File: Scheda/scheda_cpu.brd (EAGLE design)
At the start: 75 x 70 mm, 36 parts, among them IC2 LM3801N, IC3 LD1117V33

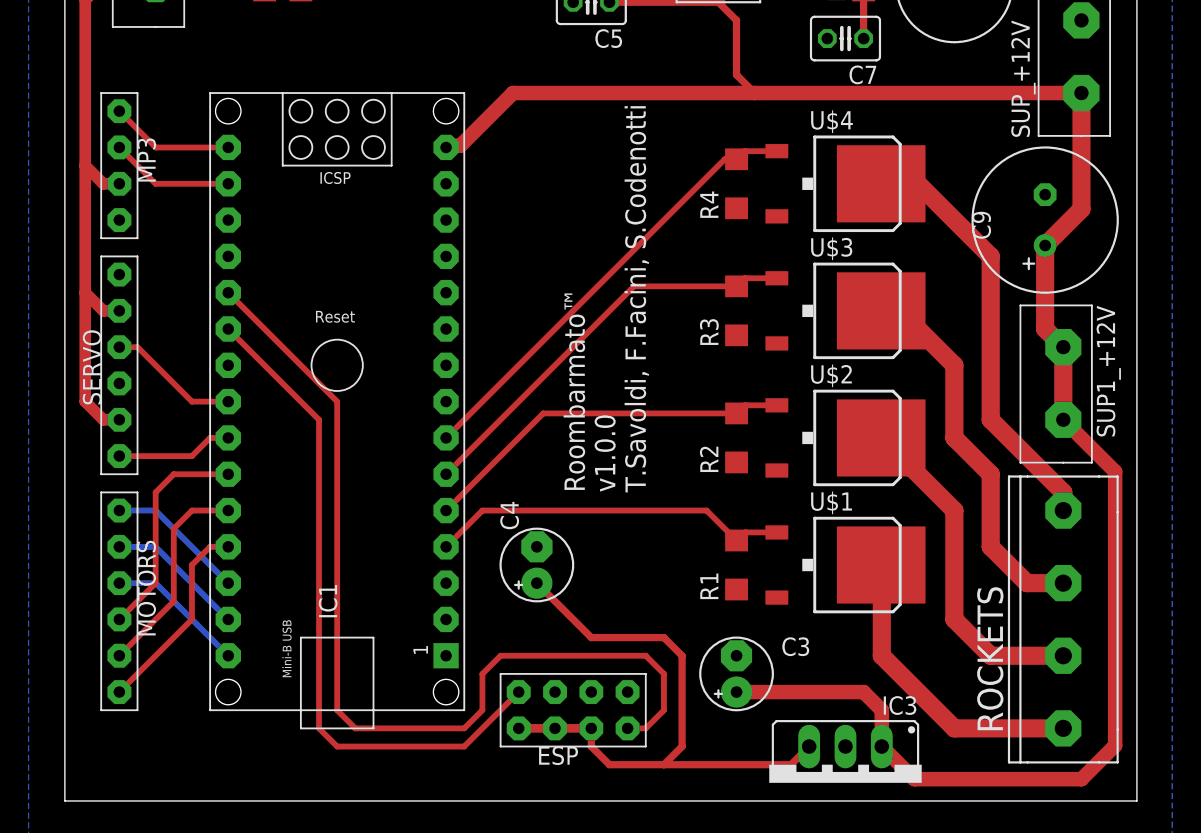
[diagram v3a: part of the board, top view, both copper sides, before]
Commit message: aggiunte etichette su pcb
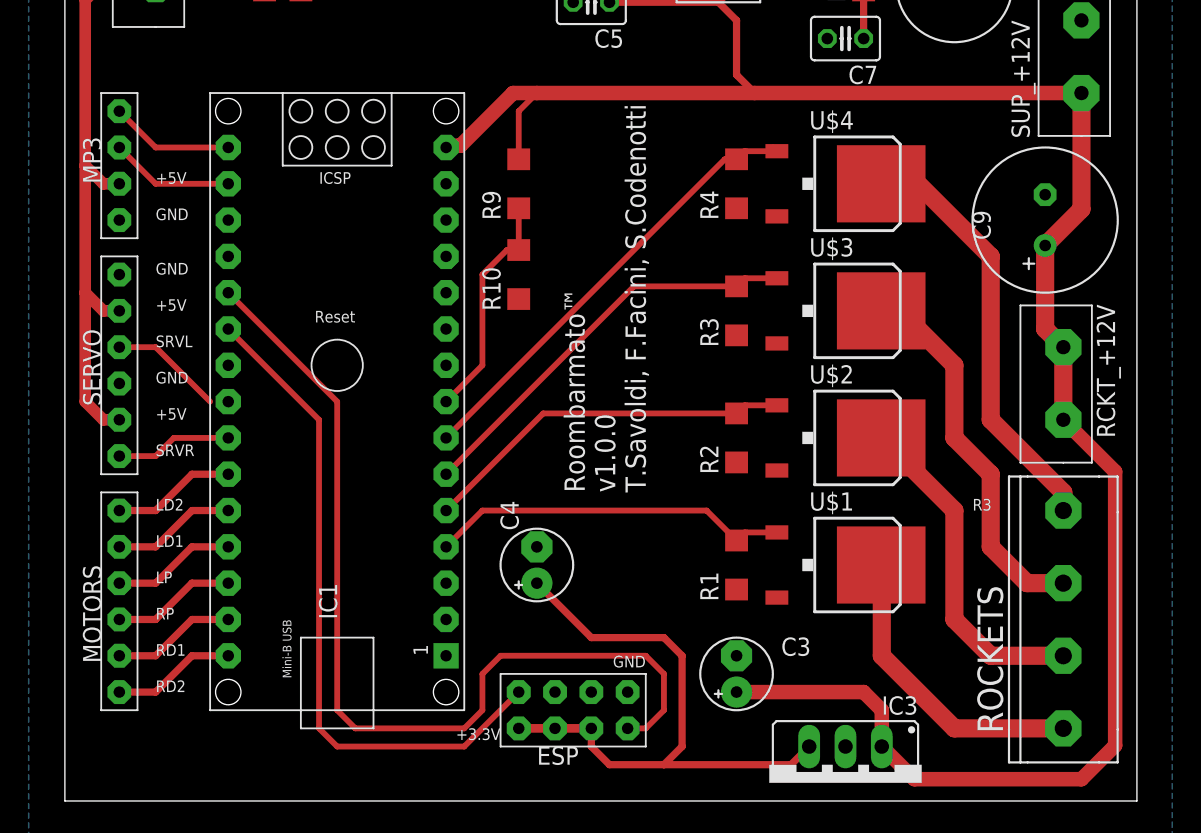
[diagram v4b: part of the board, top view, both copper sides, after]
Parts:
- added R10: 100k, roombarmato_eagle_lib:1206-RESISTOR
- added R9: 200k, roombarmato_eagle_lib:1206-RESISTOR
- turned MOTORS to 270 degrees
- renumbered SUP1_+12V to RCKT_+12V
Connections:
- net N$13 renamed LD1
- net N$16 renamed RD1
- net N$2 renamed TXD
- net N$3 renamed RXD
- net SERVO1 renamed SRV_L
- net SERVO2 renamed SRV_R
- removed net N$11: IC1.28, MOTORS.P$6
- removed net N$12: IC1.27, MOTORS.P$1
- removed net N$14: IC1.25, MOTORS.P$3
- removed net N$15: IC1.30, MOTORS.P$4
- new net CHK_VBAT: IC1.8, R10.P$2, R9.P$1
- new net LD2: IC1.25, MOTORS.P$1
- new net LP: IC1.27, MOTORS.P$3
- new net RD2: IC1.30, MOTORS.P$6
- new net RP: IC1.28, MOTORS.P$4
- net +12V: now also R9.P$2
- net GND: now also R10.P$1
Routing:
- net CHK_VBAT: track 0.00 -> 16.1 mm
- net N$14: track 15.5 -> 0.00 mm
- net N$12: track 14.1 -> 0.00 mm
- net N$15: track 9.72 -> 0.00 mm
- net N$11: track 9.72 -> 0.00 mm
- net RP: track 0.00 -> 8.67 mm
- net LP: track 0.00 -> 8.67 mm
- net RD2: track 0.00 -> 8.67 mm
- net LD2: track 0.00 -> 8.67 mm
- net LD1: track 14.8 -> 8.67 mm
- net +12V: track 149.9 -> 155.1 mm
- net SRV_L: track 9.20 -> 7.93 mm
- net RD1: track 9.72 -> 8.67 mm
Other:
- board text added: "+3.3V"
- board text added: "+5V"
- board text added: "GND"
- board text added: "LD1"
- board text added: "LD2"
- board text added: "LP"
- board text added: "R3"
- board text added: "RD1"
- board text added: "RD2"
- board text added: "RP"
- board text added: "SRVL"
- board text added: "SRVR"

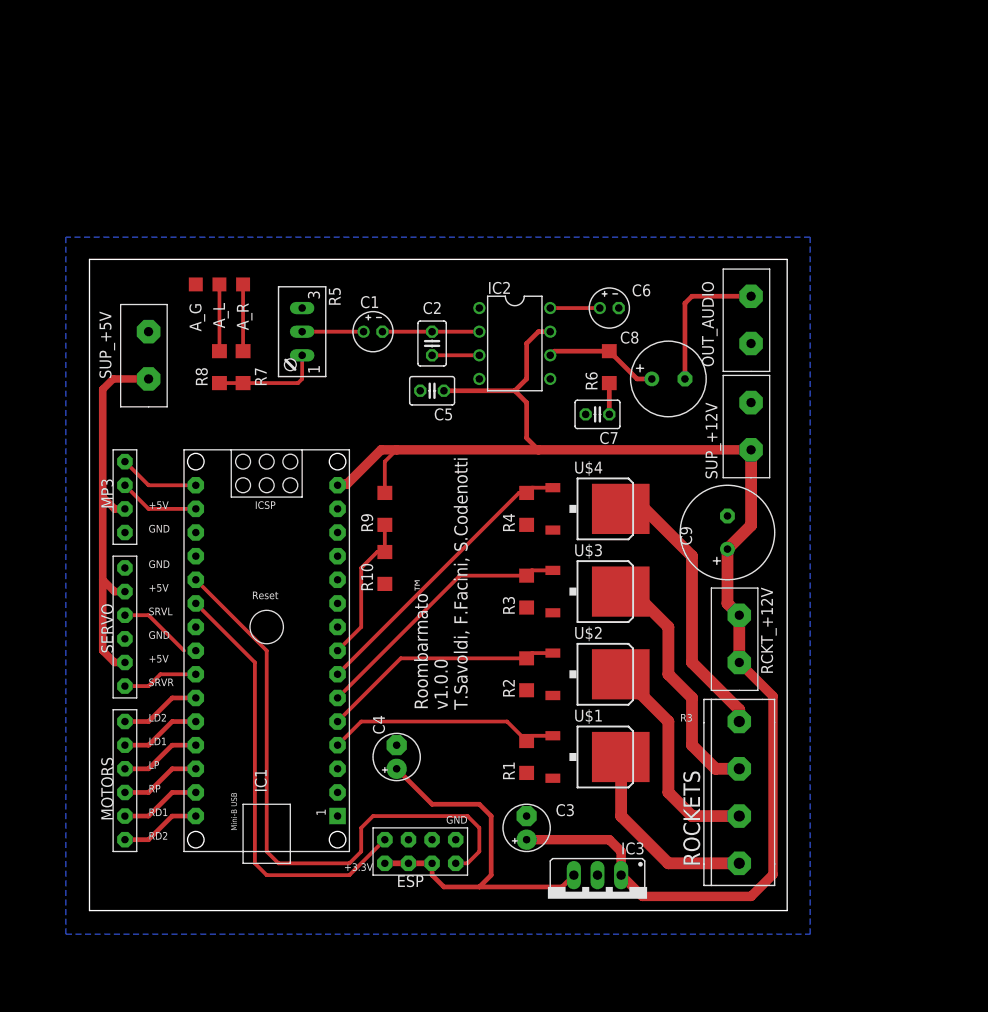
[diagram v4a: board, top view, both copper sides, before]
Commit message: create le cartelle test e ex
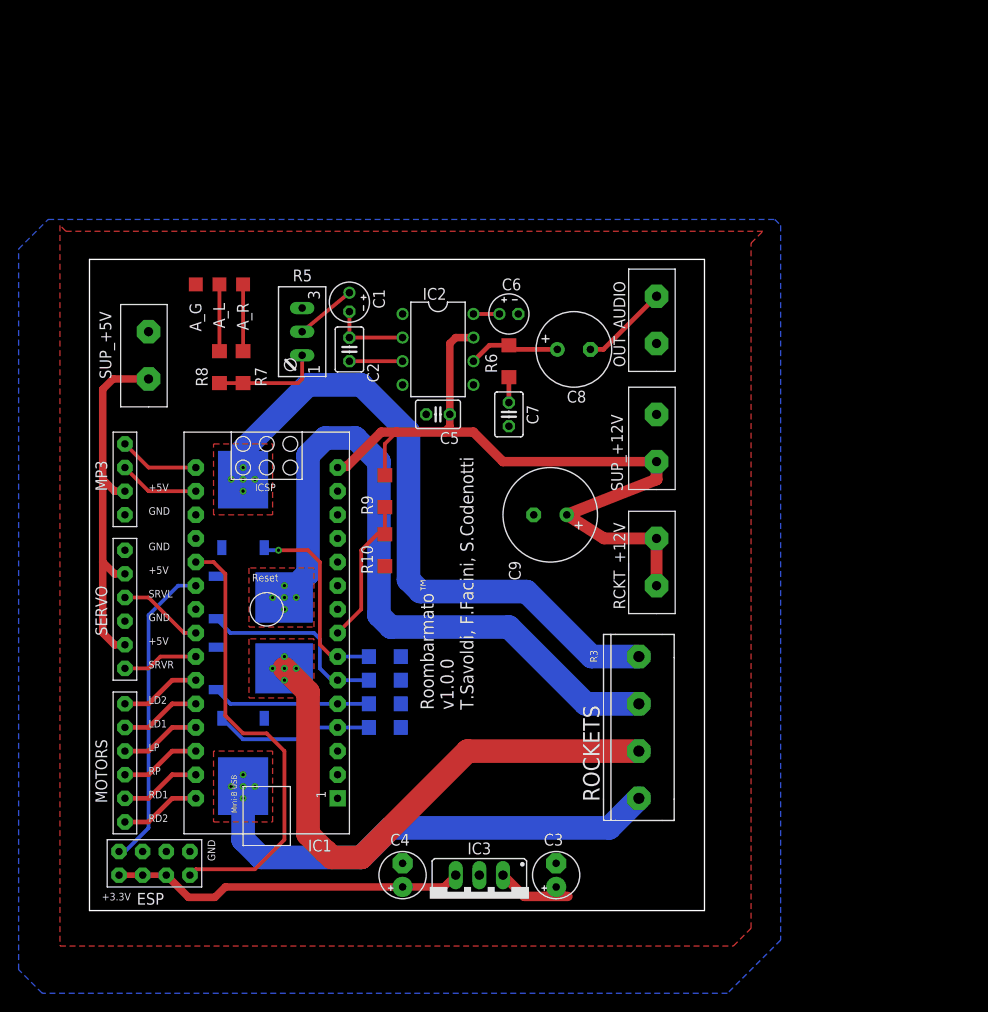
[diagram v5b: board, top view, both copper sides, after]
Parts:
- moved U$1 38.1 mm to (16.5, 15.9), flipped to the bottom, turned to 180 degrees
- moved U$4 38.1 mm to (16.5, 43.8), flipped to the bottom, turned to 0 degrees
- moved U$2 36.2 mm to (18.4, 26.0), flipped to the bottom, turned to 90 degrees
- moved U$3 36.2 mm to (18.4, 33.7), flipped to the bottom, turned to 90 degrees
- moved ESP 28.6 mm to (6.99, 5.08)
- moved R4 22.0 mm to (31.8, 27.3), flipped to the bottom, turned to 0 degrees
- moved C9 19.1 mm to (49.5, 42.5), turned to 180 degrees
- moved R3 18.0 mm to (31.8, 24.8), flipped to the bottom, turned to 0 degrees
- moved R1 15.6 mm to (31.8, 19.7), flipped to the bottom, turned to 0 degrees
- moved R2 15.6 mm to (31.8, 22.2), flipped to the bottom, turned to 0 degrees
- moved ROCKETS 12.9 mm to (59.1, 19.7)
- moved C4 12.7 mm to (33.7, 3.81)
- moved IC3 12.7 mm to (41.9, 1.27)
- moved RCKT_+12V 12.1 mm to (61.0, 34.9)
- moved R6 10.8 mm to (45.1, 59.1)
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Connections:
- new net LED: IC1.9
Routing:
- net +12V: track 155.1 -> 94.0 mm
- net R2: track 30.1 -> 74.2 mm, vias 0 -> 5
- net R3: track 31.4 -> 70.1 mm, vias 0 -> 5
- net R1: track 23.5 -> 60.2 mm, vias 0 -> 5
- net R0: track 21.2 -> 51.7 mm, vias 0 -> 5
- net N$4: track 65.5 -> 48.1 mm
- net N$1: track 46.6 -> 33.5 mm
- net C_R3: track 31.8 -> 21.3 mm, vias 0 -> 1
- net C_R1: track 26.2 -> 17.1 mm
- net C_R0: track 25.3 -> 17.3 mm
- net C_R2: track 28.8 -> 21.0 mm
- net N$17: track 15.6 -> 9.48 mm
- net +3.3V: track 43.1 -> 38.2 mm
- net N$8: track 5.33 -> 2.79 mm
- net N$10: track 12.3 -> 9.91 mm
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- added copper zone on layer 1, net +12V
- added copper zone on layer 1, net R0
- added copper zone on layer 1, net R1
- added copper zone on layer 1, net R2
- added copper zone on layer 1, net R3
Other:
- board size 75 x 70 mm -> 66.1 x 70 mm

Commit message: modificato pcb
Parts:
- added H1, H2, H3: MOUNT-HOLE3.0, ITIS:3,0
- added LED: AK500, roombarmato_eagle_lib:AK500-2
- moved U$4 37.1 mm to (52.7, 35.6), flipped to the top, turned to 270 degrees
- moved U$1 36.3 mm to (52.7, 12.7), flipped to the top, turned to 270 degrees
- moved U$2 34.8 mm to (52.7, 20.3), flipped to the top, turned to 270 degrees
- moved U$3 34.8 mm to (52.7, 27.9), flipped to the top, turned to 270 degrees
- moved R5 31.1 mm to (45.7, 81.9)
- moved A_G 31.1 mm to (35.6, 87.0)
- moved A_L 31.1 mm to (38.1, 87.0)
- moved C7 31.1 mm to (69.2, 73.0)
- moved C8 31.1 mm to (76.2, 80.0)
- moved R8 31.1 mm to (38.1, 78.1)
- moved A_R 31.1 mm to (40.6, 87.0)
- moved C1 31.1 mm to (52.1, 85.1)
- moved C2 31.1 mm to (52.1, 80.0)
- moved R6 31.1 mm to (69.2, 78.7)
- moved R7 31.1 mm to (40.6, 78.1)
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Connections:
- net CHK_VBAT: now also IC1.9; no longer IC1.8
- net GND: now also LED.P$1
- net LED: now also IC1.8, LED.P$2; no longer IC1.9
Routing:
- net +12V: track 94.0 -> 5.42 mm
- net LED: track 0.00 -> 77.1 mm
- net R3: track 70.1 -> 35.9 mm
- net R2: track 74.2 -> 41.2 mm
- net R1: track 60.2 -> 40.0 mm
- net N$4: track 48.1 -> 68.1 mm
- net N$1: track 33.5 -> 50.4 mm
- net C_R3: track 21.3 -> 36.7 mm
- net +3.3V: track 38.2 -> 24.4 mm
- net RXD: track 8.67 -> 19.6 mm
- net C_R2: track 21.0 -> 31.6 mm, vias 0 -> 1
- net TXD: track 8.67 -> 18.5 mm
- net R0: track 51.7 -> 42.4 mm
- net C_R1: track 17.1 -> 26.0 mm, vias 0 -> 1
- net SRV_L: track 9.20 -> 17.4 mm
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- added copper zone on layer 16, net +12V
- added copper zone on layer 1, net GND
- removed copper zone on layer 1, net +12V
- removed copper zone on layer 16, net GND
- removed copper zone on layer 1, net R0
- removed copper zone on layer 1, net R1
- removed copper zone on layer 1, net R2
- removed copper zone on layer 1, net R3
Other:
- board size 66.1 x 70 mm -> 90 x 90 mm

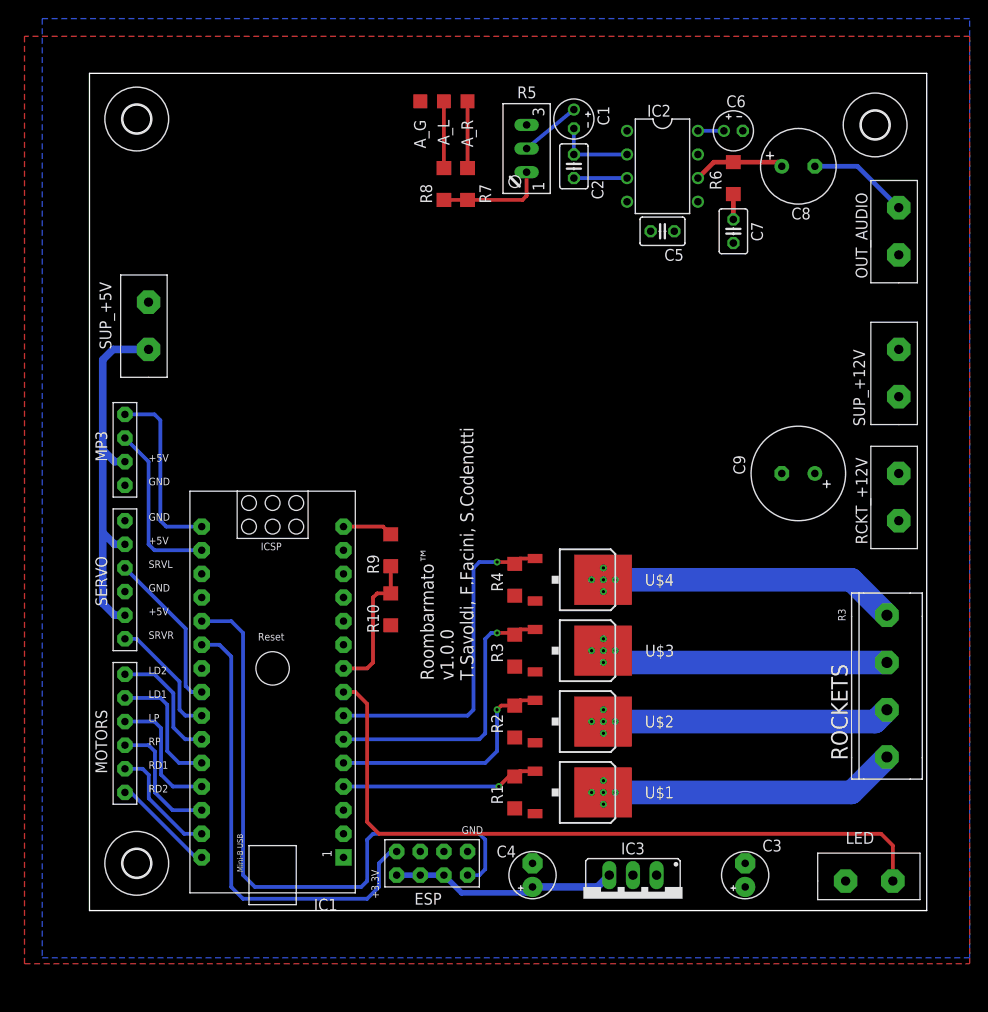
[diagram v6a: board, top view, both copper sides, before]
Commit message: modificato leggermente pcb, cambiato package lm380
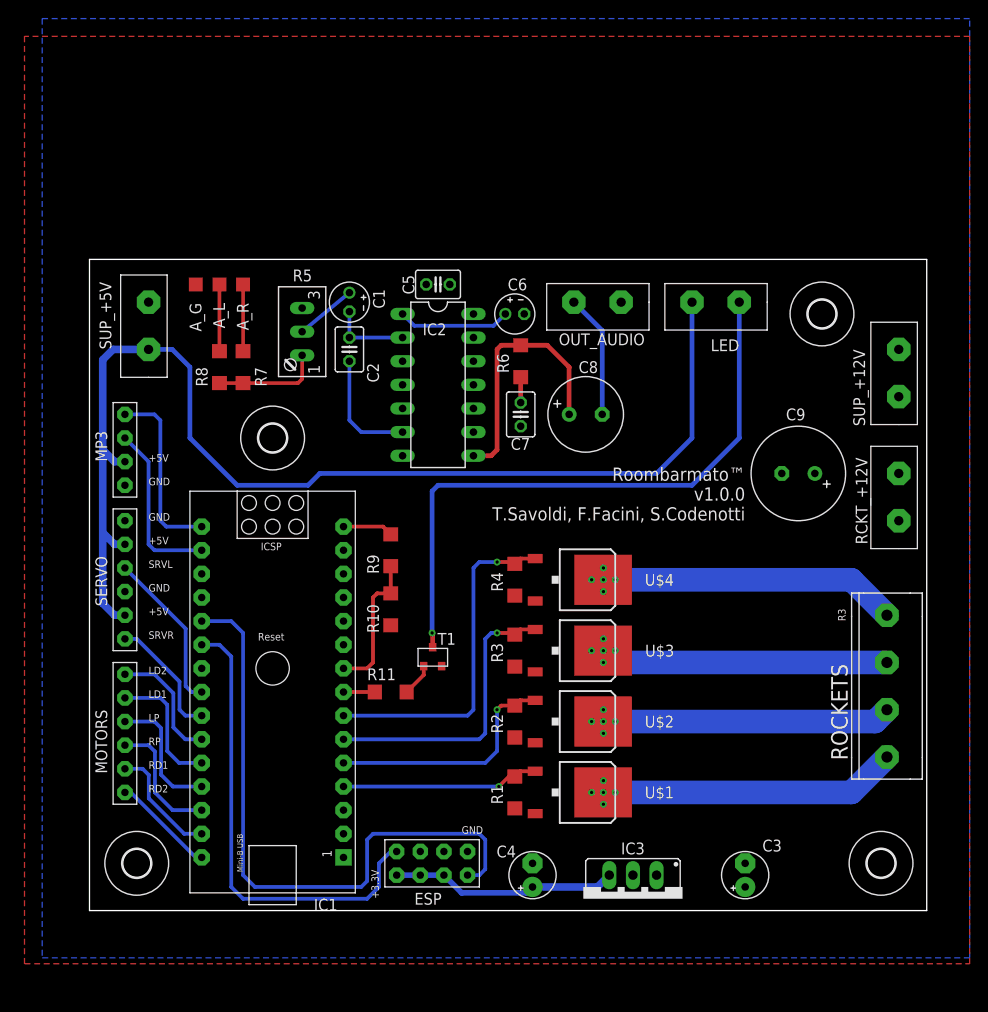
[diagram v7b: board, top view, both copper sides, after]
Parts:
- added H4: MOUNT-HOLE3.0, ITIS:3,0
- added R11: 1k, roombarmato_eagle_lib:1206-RESISTOR
- added T1: BC-817, CiniTechLibrary:SOT-23
- IC2: value LM3801N -> LM380; device roombarmato_eagle_lib:DIL08 -> roombarmato_eagle_lib:DIL14
- moved LED 63.3 mm to (69.8, 65.4), turned to 180 degrees
- moved H3 37.3 mm to (19.7, 50.8)
- moved C8 35.1 mm to (53.3, 53.3)
- moved IC2 33.7 mm to (37.5, 56.5)
- moved R5 31.1 mm to (21.6, 62.2)
- moved A_G 31.1 mm to (11.4, 67.3)
- moved A_L 31.1 mm to (14.0, 67.3)
- moved R8 31.1 mm to (14.0, 58.4)
- moved A_R 31.1 mm to (16.5, 67.3)
- moved C1 31.1 mm to (27.9, 65.4)
- moved C2 31.1 mm to (27.9, 60.3)
- moved R7 31.1 mm to (16.5, 58.4)
- moved C6 30.7 mm to (45.7, 64.1)
- moved OUT_AUDIO 30.3 mm to (57.1, 65.4), turned to 180 degrees
- moved C7 30.2 mm to (46.4, 53.3)
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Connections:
- new net N$2: LED.P$1, T1.P$3
- new net N$3: R11.P$2, T1.P$2
- net +12V: now also IC2.14; no longer IC2.7
- net +5V: now also LED.P$2
- net GND: now also IC2.10, IC2.11, IC2.12, IC2.3, IC2.4, IC2.7, T1.P$1; no longer LED.P$1
- net LED: now also R11.P$1; no longer LED.P$2
- net N$10: now also IC2.8; no longer IC2.6
- net N$7: now also IC2.6; no longer IC2.3
- net N$8: now also IC2.1; no longer IC2.8
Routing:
- net +5V: track 40.3 -> 126.0 mm
- net LED: track 77.1 -> 3.37 mm
- net N$2: track 0.00 -> 66.8 mm, vias 0 -> 1
- net N$10: track 9.91 -> 27.6 mm
- net N$8: track 2.79 -> 12.1 mm
- net N$7: track 5.71 -> 12.6 mm
- net N$3: track 0.00 -> 3.54 mm
- net N$17: track 10.9 -> 13.3 mm
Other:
- board size 90 x 90 mm -> 90 x 70 mm

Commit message: sistemato pcb
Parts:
- removed C4: (no value), roombarmato_eagle_lib:E2,5-5
- removed OUT_AUDIO, RCKT_+12V, SUP_+12V, SUP_+5V: AK500, roombarmato_eagle_lib:AK500-2
- added C10: 100nF, ITIS:C025-030X050
- added C11: 10uF, ITIS:E2-4
- added OUT-AUDIO, RCKT-12, SUP-12, SUP-5, SWITCH: MORSETTIERE-2, CyberLibrary:MORSETTIERE-2
- C3: value (none) -> 22uF; device roombarmato_eagle_lib:E2,5-5 -> ITIS:E2-4
- IC3: value LD1117V33 -> AMS1117-3.3V; device roombarmato_eagle_lib:78XXS -> roombarmato_eagle_lib:SOT223
- LED: value AK500 -> MORSETTIERE-2; device roombarmato_eagle_lib:AK500-2 -> CyberLibrary:MORSETTIERE-2
- moved C3 20.4 mm to (50.2, 5.08)
- moved IC3 3.81 mm to (58.4, 5.08), turned to 270 degrees
- moved R11 2.62 mm to (31.8, 26.0)
- moved H4 2.54 mm to (85.1, 7.62)
- moved C9 1.27 mm to (74.9, 47.0)
- moved LED 1.27 mm to (68.6, 65.4), turned to 0 degrees
- renumbered U$1 to T2, U$2 to T3, U$3 to T4, U$4 to T5
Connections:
- removed net N$17: C8.-, OUT_AUDIO.P$2
- new net N$11: C8.-, OUT-AUDIO.B
- new net SWITCH: IC1.8, SWITCH.B
- net +12V: now also RCKT-12.A, RCKT-12.B, SUP-12.A; no longer C3.+, IC3.IN, RCKT_+12V.P$1, RCKT_+12V.P$2, SUP_+12V.P$1
- net +3.3V: now also C10.1, C3.+, IC3.2; no longer C4.+, IC3.OUT
- net +5V: now also C11.+, IC3.3, LED.A, SUP-5.A; no longer LED.P$2, SUP_+5V.P$1
- net CHK_VBAT: now also IC1.10; no longer IC1.9
- net GND: now also C10.2, C11.-, IC3.1, OUT-AUDIO.A, SUP-12.B, SUP-5.B, SWITCH.A; no longer C4.-, IC3.GND, OUT_AUDIO.P$1, SUP_+12V.P$2, SUP_+5V.P$2
- net LED: now also IC1.9; no longer IC1.8
- net N$2: now also LED.B; no longer LED.P$1
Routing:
- net +5V: track 126.0 -> 227.9 mm
- net SWITCH: track 0.00 -> 62.6 mm
- net N$11: track 0.00 -> 13.4 mm
- net N$17: track 13.3 -> 0.00 mm
- net +3.3V: track 24.4 -> 27.3 mm
- net CHK_VBAT: track 15.4 -> 12.9 mm
- net N$10: track 27.6 -> 25.2 mm
- net N$3: track 3.54 -> 2.56 mm
- net N$2: track 66.8 -> 67.7 mm
- net LED: track 3.37 -> 2.73 mm
